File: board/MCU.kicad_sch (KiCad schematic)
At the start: 15 parts, among them Q1 NMOS, U4 LT1910, U7 ESP32-S2-DEVKITM-1U

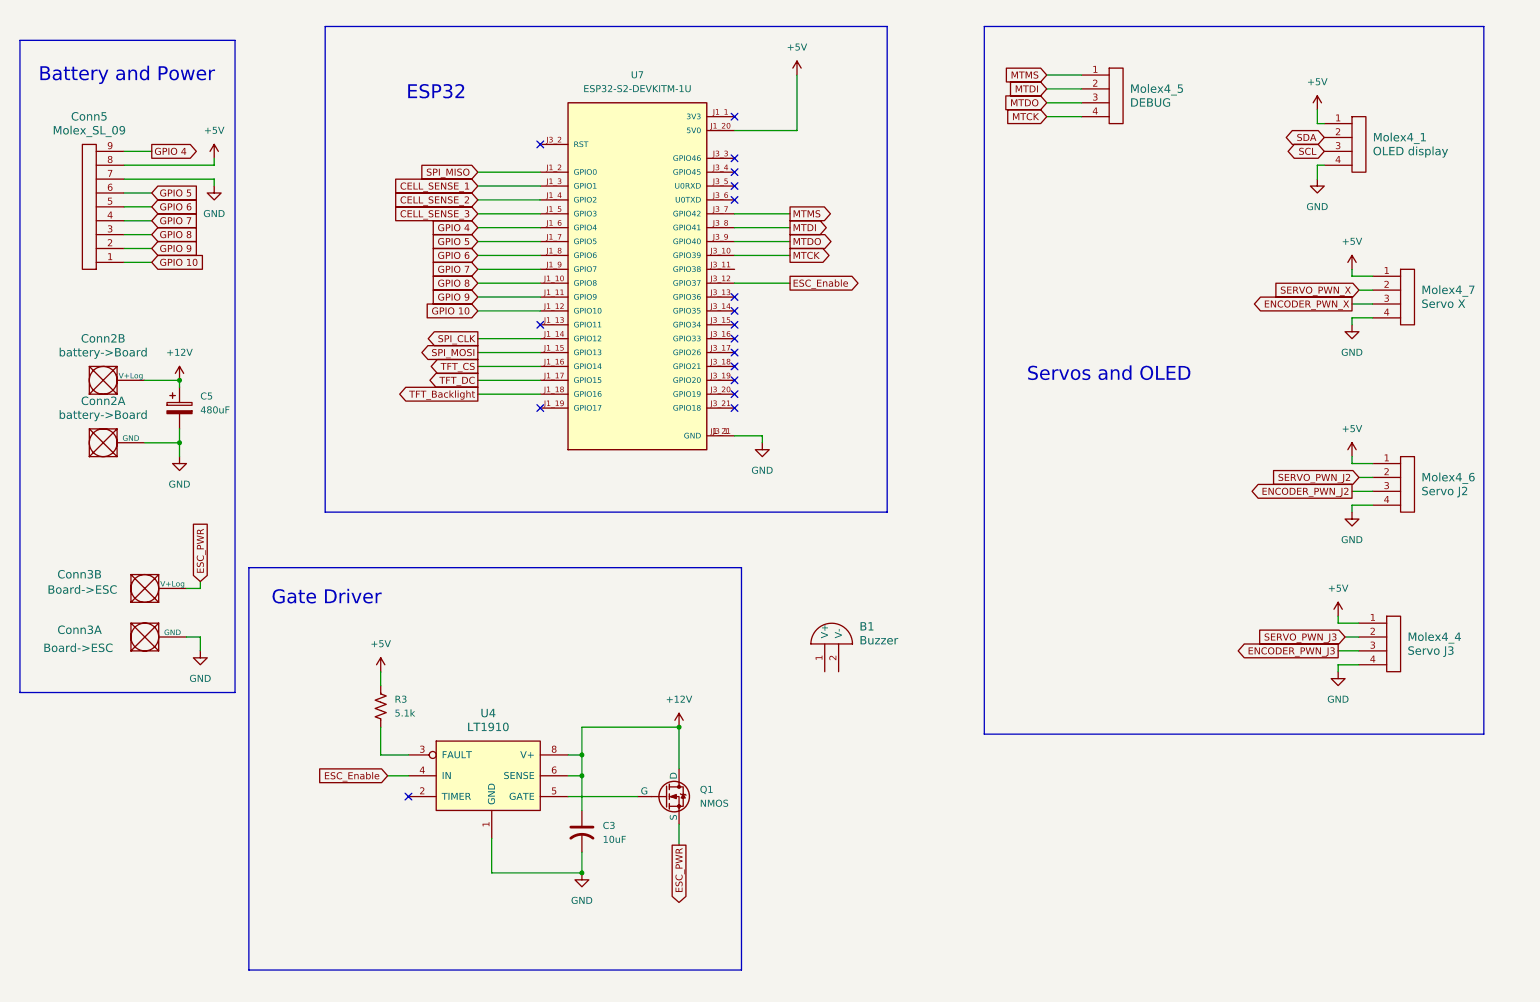
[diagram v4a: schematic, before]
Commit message: named pins + OLED pinout added
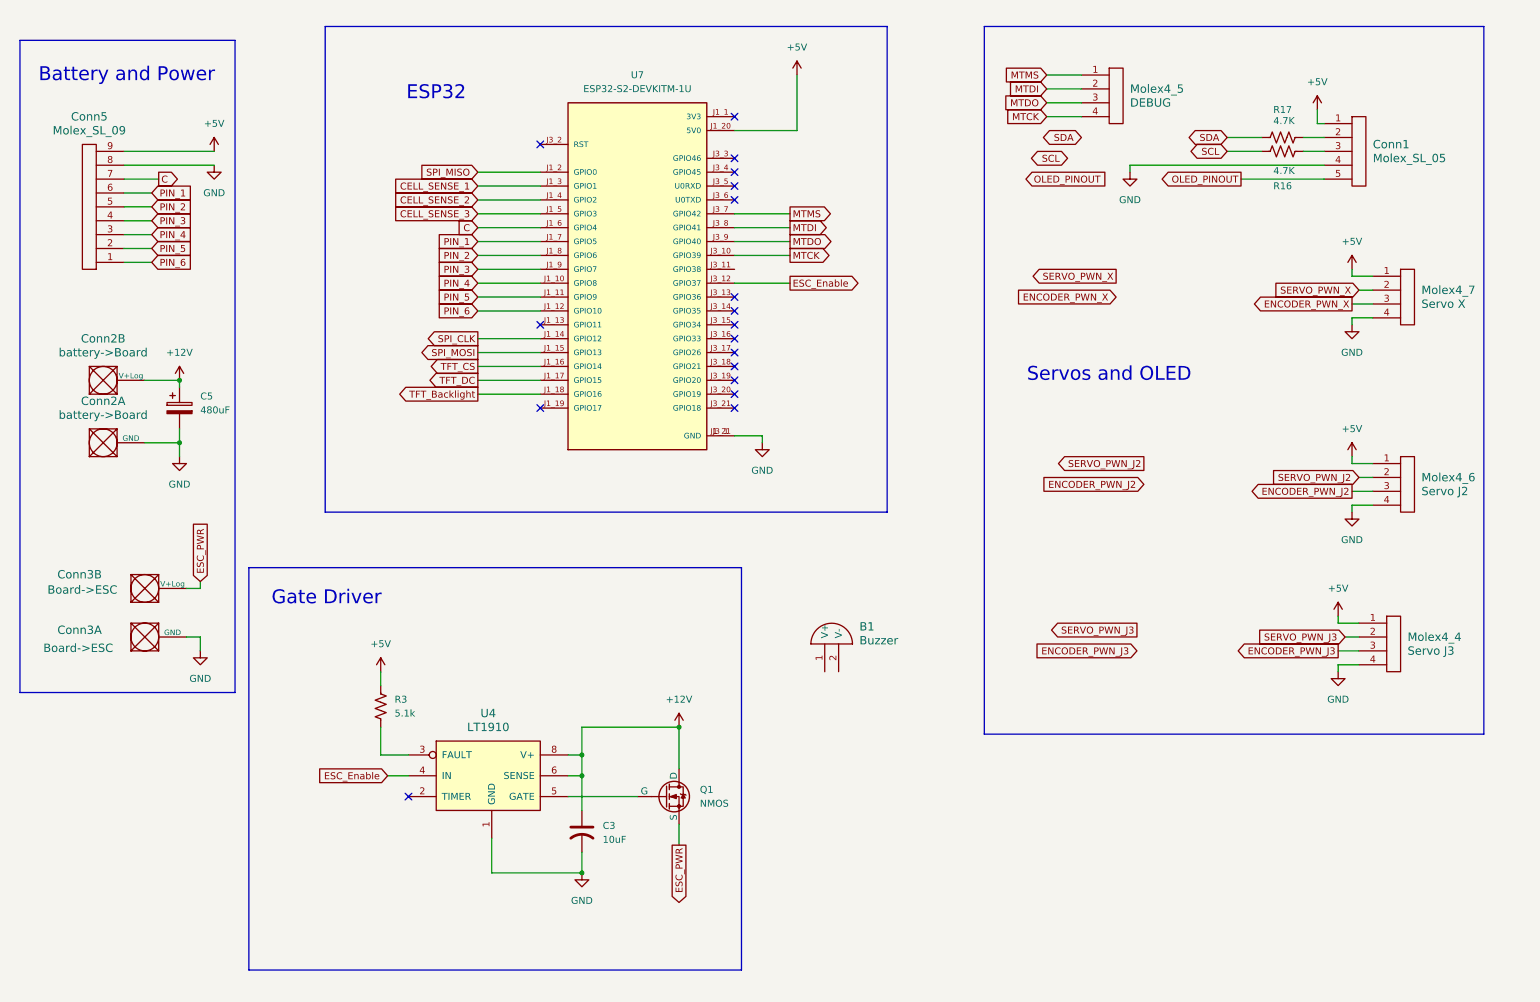
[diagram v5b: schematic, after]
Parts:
- removed Molex4_1: OLED display, MRDT_Connectors:MOLEX_SL_04_Vertical, symbol MRDT_Connectors:Molex_SL_04
- added Conn1: Molex_SL_05, symbol MRDT_Connectors:Molex_SL_05
- added R16, R17: 4.7K, symbol Device:R_US
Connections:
- net +5V: now also Conn5.9, Conn1.1; no longer Conn5.8
- net GND: now also Conn5.8, Conn1.4; no longer Conn5.7
- net SCL: now also R16.2
- net SDA: now also R17.1
- net GPIO 10 renamed PIN_6
- net GPIO 4 renamed C
- net C: now also Conn5.7; no longer Conn5.9
- net GPIO 5 renamed PIN_1
- net GPIO 6 renamed PIN_2
- net GPIO 7 renamed PIN_3
- net GPIO 8 renamed PIN_4
- net GPIO 9 renamed PIN_5
- new net: Conn1.3, R16.1
- new net: Conn1.2, R17.2
- new net OLED_PINOUT: Conn1.5

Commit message: fixed tags added buzzer
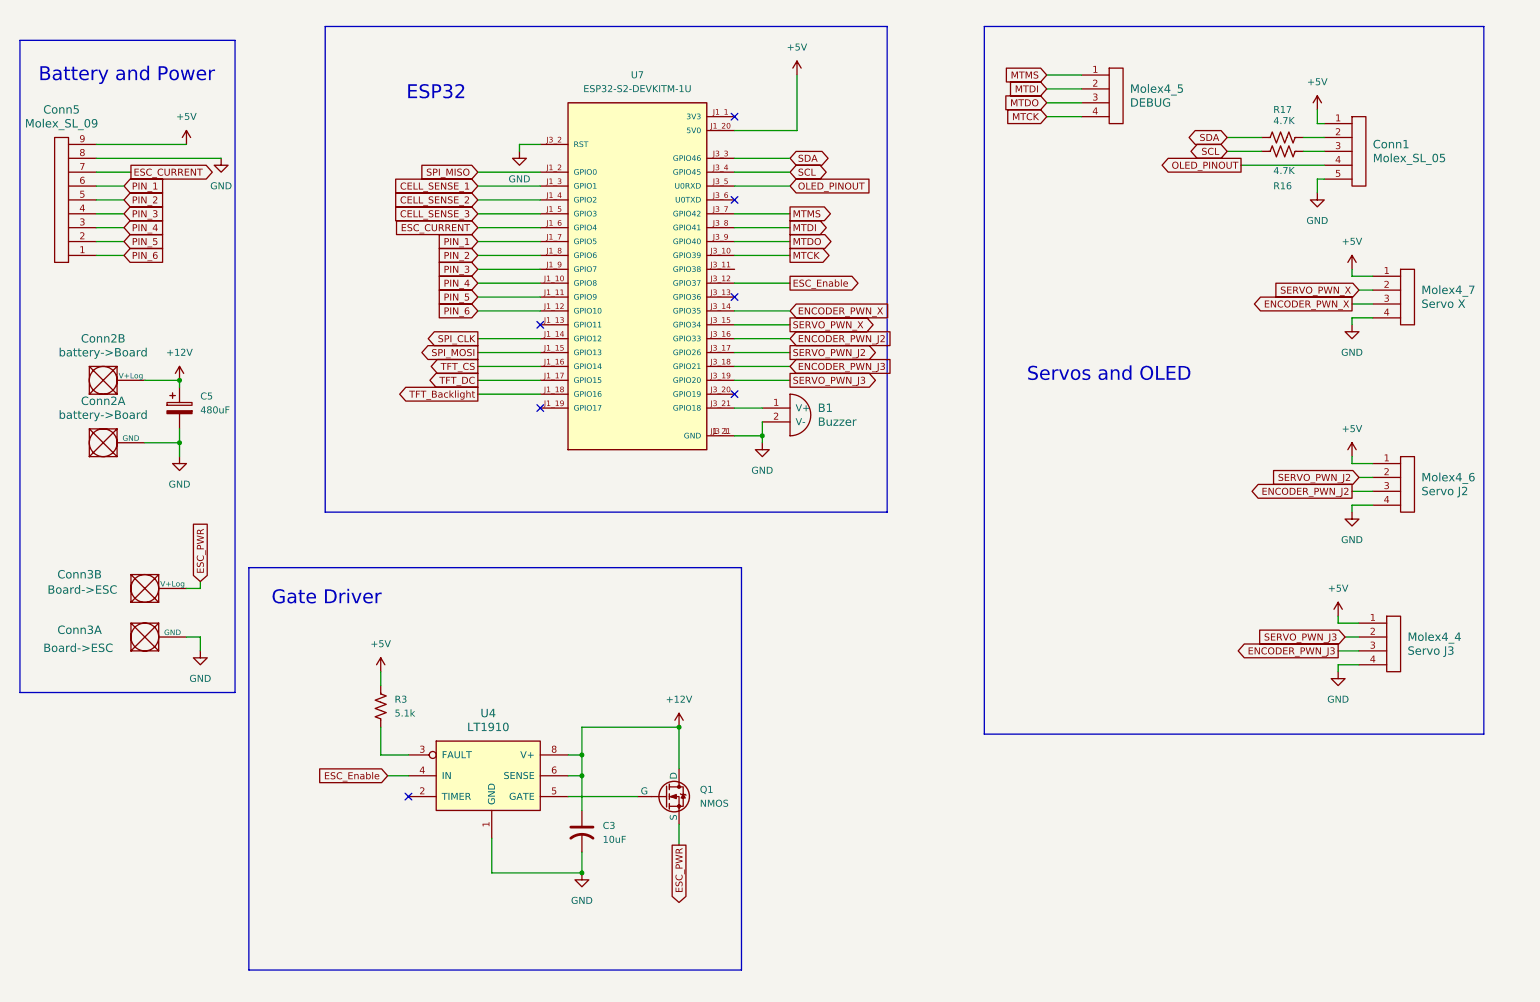
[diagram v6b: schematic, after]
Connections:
- net ENCODER_PWN_J2: now also U7.J3_16 (GPIO33)
- net ENCODER_PWN_J3: now also U7.J3_18 (GPIO21)
- net ENCODER_PWN_X: now also U7.J3_14 (GPIO35)
- net GND: now also B1.2 (V-), Conn1.5, U7.J3_2 (RST); no longer Conn1.4
- net OLED_PINOUT: now also Conn1.4, U7.J3_5 (U0RXD); no longer Conn1.5
- net SCL: now also U7.J3_4 (GPIO45)
- net SDA: now also U7.J3_3 (GPIO46)
- net SERVO_PWN_J2: now also U7.J3_17 (GPIO26)
- net SERVO_PWN_J3: now also U7.J3_19 (GPIO20)
- net SERVO_PWN_X: now also U7.J3_15 (GPIO34)
- net at B1.1 (V+): now also U7.J3_21 (GPIO18)
- net C renamed ESC_CURRENT
- no-connect marks 18 -> 7
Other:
- moved on the sheet: B1, Conn5

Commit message: Add Buzzer, moved PWM pins
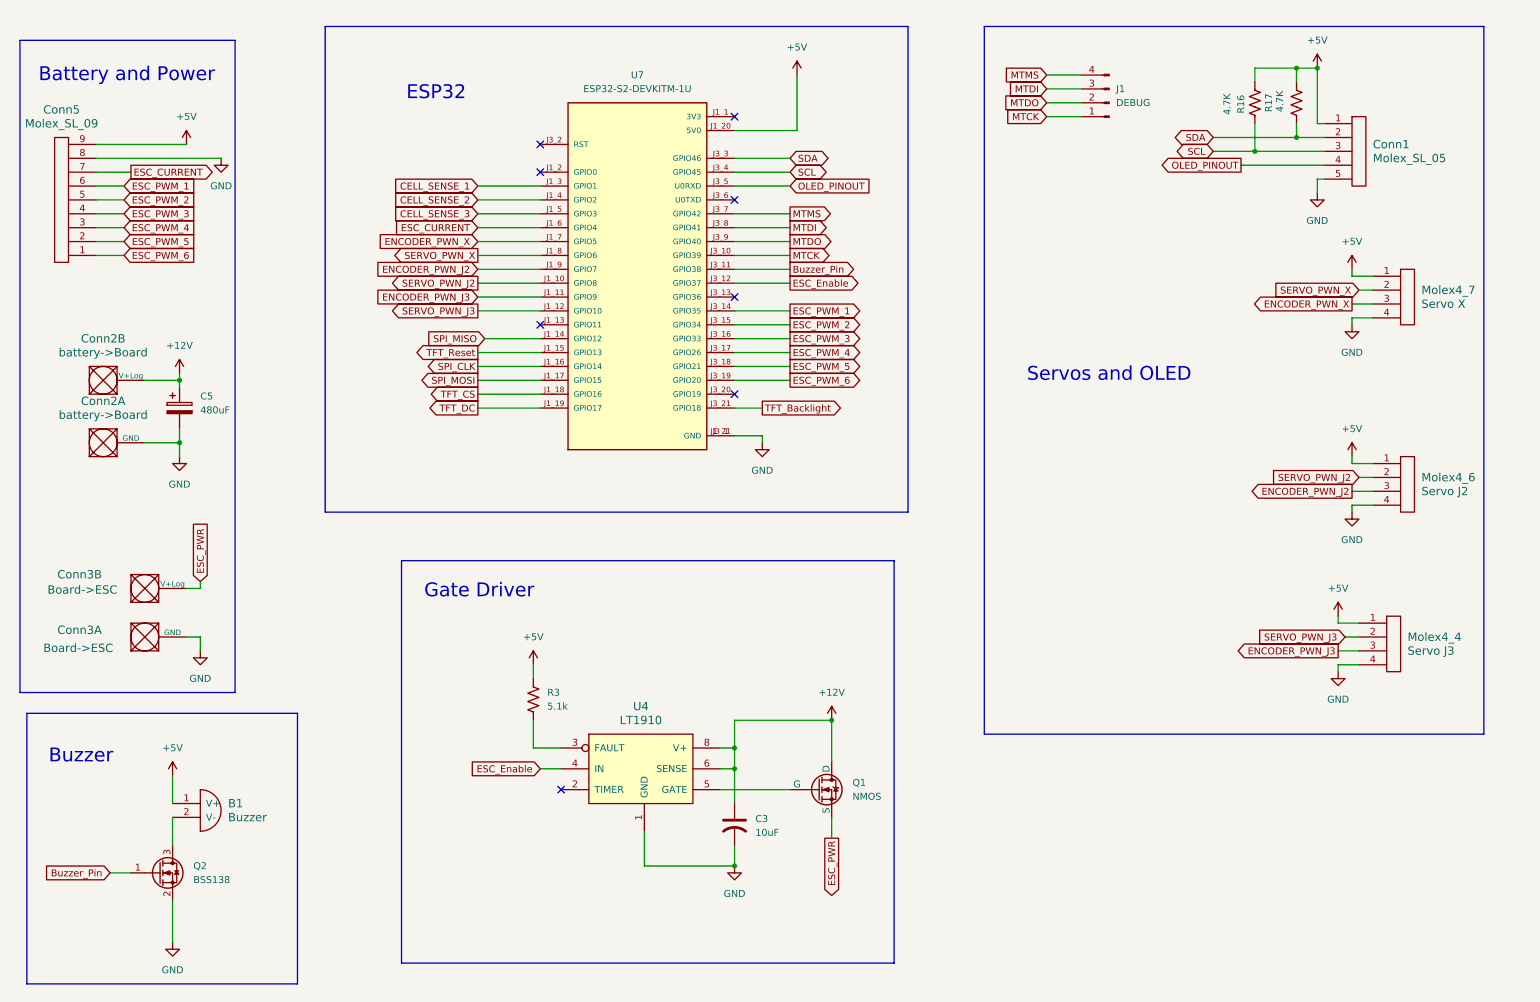
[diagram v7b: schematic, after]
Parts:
- removed Molex4_5: DEBUG, MRDT_Connectors:MOLEX_SL_04_Vertical, symbol MRDT_Connectors:Molex_SL_04
- added J1: DEBUG, symbol Connector:Conn_01x04_Pin
- added Q2: BSS138, Package_TO_SOT_SMD:SOT-23, symbol Transistor_FET:BSS138
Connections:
- net +5V: now also B1.1 (V+), R16.1, R17.2
- net ENCODER_PWN_J2: now also U7.J1_9 (GPIO7); no longer U7.J3_16 (GPIO33)
- net ENCODER_PWN_J3: now also U7.J1_11 (GPIO9); no longer U7.J3_18 (GPIO21)
- net ENCODER_PWN_X: now also U7.J1_7 (GPIO5); no longer U7.J3_14 (GPIO35)
- net GND: now also Q2.2 (S); no longer B1.2 (V-), U7.J3_2 (RST)
- net MTCK: now also J1.1 (Pin_1)
- net MTDI: now also J1.3 (Pin_3)
- net MTDO: now also J1.2 (Pin_2)
- net MTMS: now also J1.4 (Pin_4)
- net SCL: now also Conn1.3
- net SDA: now also Conn1.2
- net SERVO_PWN_J2: now also U7.J1_10 (GPIO8); no longer U7.J3_17 (GPIO26)
- net SERVO_PWN_J3: now also U7.J1_12 (GPIO10); no longer U7.J3_19 (GPIO20)
- net SERVO_PWN_X: now also U7.J1_8 (GPIO6); no longer U7.J3_15 (GPIO34)
- net SPI_CLK: now also U7.J1_16 (GPIO14); no longer U7.J1_14 (GPIO12)
- net SPI_MISO: now also U7.J1_14 (GPIO12); no longer U7.J1_2 (GPIO0)
- net SPI_MOSI: now also U7.J1_17 (GPIO15); no longer U7.J1_15 (GPIO13)
- net TFT_Backlight: now also U7.J3_21 (GPIO18); no longer U7.J1_18 (GPIO16)
- net TFT_CS: now also U7.J1_18 (GPIO16); no longer U7.J1_16 (GPIO14)
- net TFT_DC: now also U7.J1_19 (GPIO17); no longer U7.J1_17 (GPIO15)
- net Buzzer_Pin: now reaches U7.J3_11 (GPIO38)
- net Buzzer_Pin: now also Q2.1 (G)
- net PIN_1 renamed ESC_PWM_1
- net ESC_PWM_1: now also U7.J3_14 (GPIO35); no longer U7.J1_7 (GPIO5)
- net PIN_2 renamed ESC_PWM_2
- net ESC_PWM_2: now also U7.J3_15 (GPIO34); no longer U7.J1_8 (GPIO6)
- net PIN_3 renamed ESC_PWM_3
- net ESC_PWM_3: now also U7.J3_16 (GPIO33); no longer U7.J1_9 (GPIO7)
- net PIN_4 renamed ESC_PWM_4
- net ESC_PWM_4: now also U7.J3_17 (GPIO26); no longer U7.J1_10 (GPIO8)
- net PIN_5 renamed ESC_PWM_5
- net ESC_PWM_5: now also U7.J3_18 (GPIO21); no longer U7.J1_11 (GPIO9)
- net PIN_6 renamed ESC_PWM_6
- net ESC_PWM_6: now also U7.J3_19 (GPIO20); no longer U7.J1_12 (GPIO10)
- new net: B1.2 (V-), Q2.3 (D)
- new net TFT_Reset: U7.J1_15 (GPIO13)
- no-connect marks 7 -> 8
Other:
- note added: "Buzzer"
- moved on the sheet: B1, C3, Q1, R16, R17, R3, U4

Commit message: Schematic Finished
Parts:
- removed Conn1: Molex_SL_05, symbol MRDT_Connectors:Molex_SL_05
- added Conn6: Molex_SL_07, symbol MRDT_Connectors:Molex_SL_07
- added Molex4_1: I2C_BUS, MRDT_Connectors:MOLEX_SL_04_Vertical, symbol MRDT_Connectors:Molex_SL_04
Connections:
- net +5V: now also Molex4_1.1
- net GND: now also Molex4_1.4
- net SCL: now also Molex4_1.3
- net SDA: now also Molex4_1.2
- net SPI_CLK: now also Conn6.3
- net SPI_MISO: now also Conn6.1
- net SPI_MOSI: now also Conn6.4
- net TFT_Backlight: now also Conn6.7
- net TFT_CS: now also Conn6.5
- net TFT_DC: now also Conn6.6
- net TFT_Reset: now also Conn6.2
- net OLED_PINOUT: no longer names the net of U7.J3_5 (U0RXD)
- no-connect marks 8 -> 9
